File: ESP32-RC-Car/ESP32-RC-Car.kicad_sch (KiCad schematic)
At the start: 4 parts, among them J1 Conn_01x02, U1 L298N, U2 ESP32

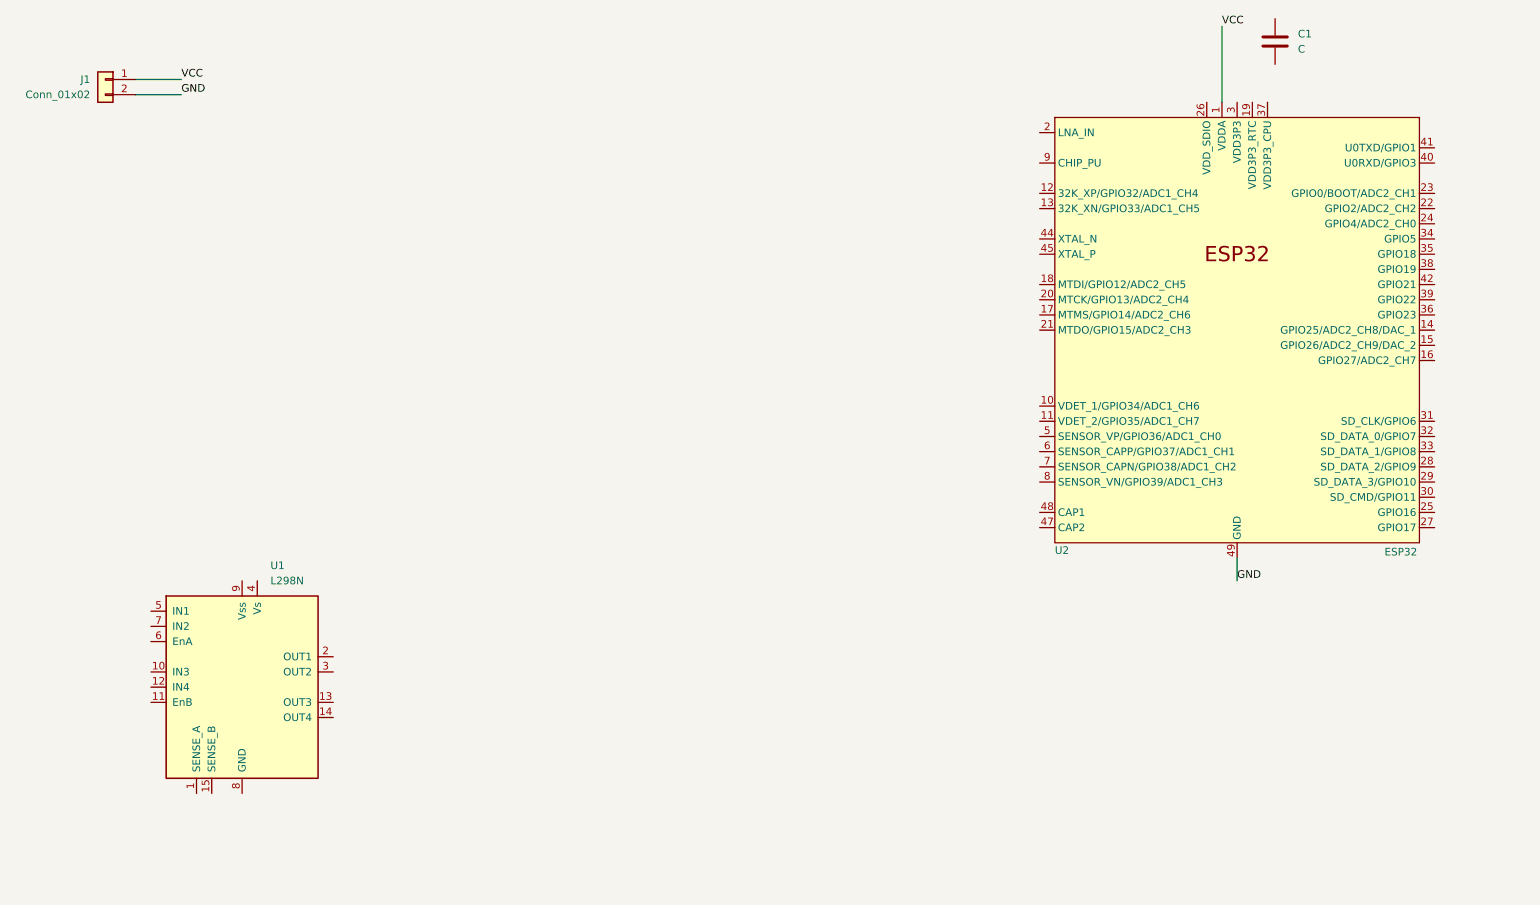
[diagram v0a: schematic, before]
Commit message: Finished MCU Power Supply Section
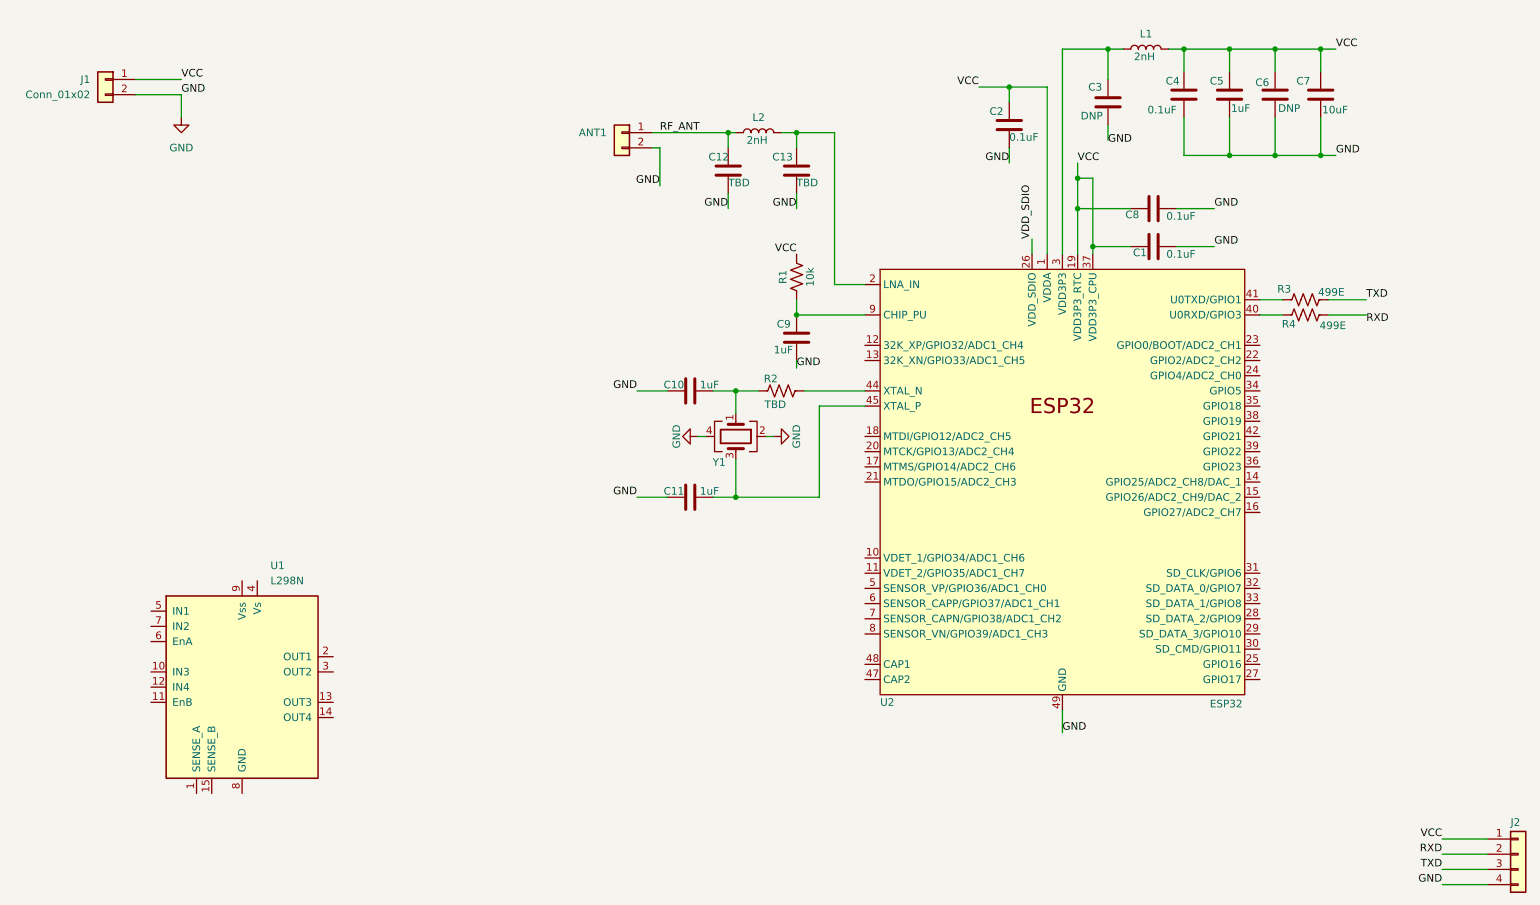
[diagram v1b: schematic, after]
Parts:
- added ANT1: Conn_01x02, symbol Connector_Generic:Conn_01x02
- added C10, C11, C5, C9: 1uF, symbol Device:C
- added C12, C13: TBD, symbol Device:C
- added C2, C4, C8: 0.1uF, symbol Device:C
- added C3, C6: DNP, symbol Device:C
- added C7: 10uF, symbol Device:C
- added J2: (no value), symbol Connector_Generic:Conn_01x04
- added L1, L2: 2nH, symbol Device:L
- added R1: 10k, symbol Device:R_US
- added R2: TBD, symbol Device:R_US
- added R3, R4: 499E, symbol Device:R_US
- added Y1: Crystal_GND24, symbol Device:Crystal_GND24
- C1: value C -> 0.1uF
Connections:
- net GND: now also C1.2, ANT1.2 (Pin_2), C10.2, C11.2, C12.1, C13.1, C2.1, C3.1, C4.1, C5.1, C6.1, C7.1, C8.2, C9.1, J2.4 (Pin_4), Y1.2, Y1.4
- net VCC: now also C1.1, U2.19 (VDD3P3_RTC), U2.37 (VDD3P3_CPU), C2.2, C4.2, C5.2, C6.2, C7.2, C8.1, J2.1 (Pin_1), L1.2, R1.2
- net at U2.2 (LNA_IN): now also C13.2, L2.2
- net VDD_SDIO: now reaches U2.26 (VDD_SDIO)
- net at U2.3 (VDD3P3), U2.4 (VDD3P3): now also C3.2, L1.1
- net at U2.40 (U0RXD/GPIO3): now also R4.2
- net at U2.41 (U0TXD/GPIO1): now also R3.2
- net at U2.44 (XTAL_N): now also R2.1
- net at U2.45 (XTAL_P): now also C11.1, Y1.3
- net at U2.9 (CHIP_PU): now also C9.2, R1.1
- new net: C10.1, R2.2, Y1.1
- new net RF_ANT: ANT1.1 (Pin_1), C12.2, L2.1
- new net RXD: J2.2 (Pin_2), R4.1
- new net TXD: J2.3 (Pin_3), R3.1
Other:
- moved on the sheet: C1, U2
